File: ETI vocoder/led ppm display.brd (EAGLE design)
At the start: 49.2 x 51.4 mm, 29 parts, among them IC1 TL082P, IC2 LM3915N

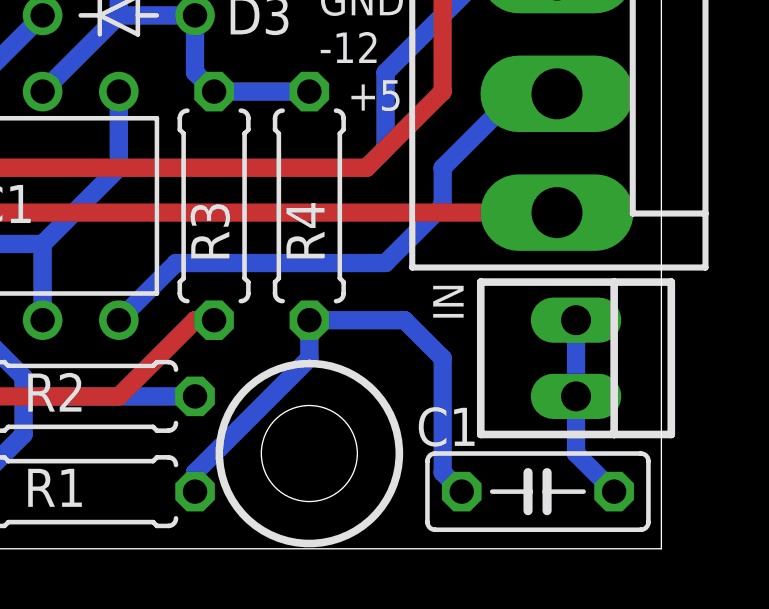
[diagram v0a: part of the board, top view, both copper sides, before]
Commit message: All ETI boards checked for caps and pots
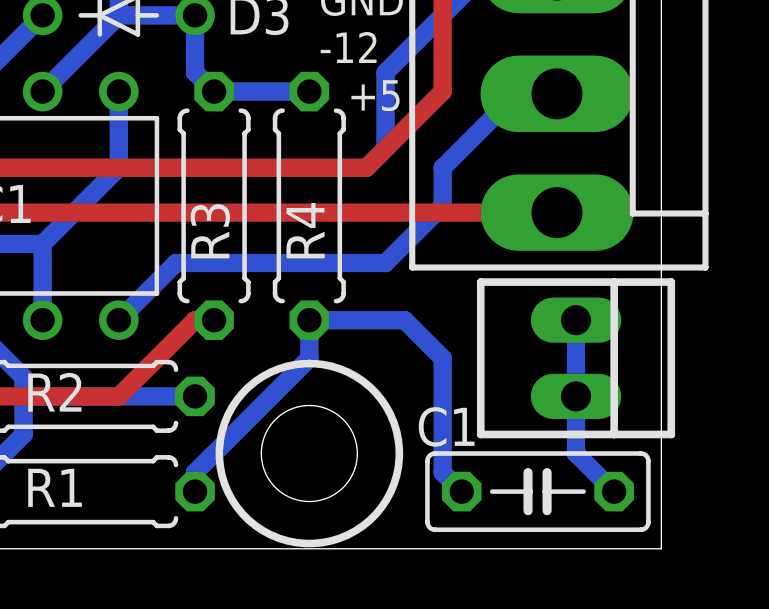
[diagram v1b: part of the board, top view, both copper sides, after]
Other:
- board text added: "+12V"
- board text added: "+5V"
- board text added: "-12V"
- board text added: "ETI Vocoder"
- board text added: "Input"
- board text added: "LED PPM v1.0"
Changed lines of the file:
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@@
 <?xml version="1.0" encoding="utf-8"?>
 <!DOCTYPE eagle SYSTEM "eagle.dtd">
-<eagle version="7.2.0">
+<eagle version="6.2">
 <drawing>
 <settings>
@@
 <setting verticaltext="up"/>
 </settings>
-<grid distance="0.0125" unitdist="inch" unit="mm" style="dots" multiple="1" display="yes" altdistance="0.025" altunitdist="inch" altunit="inch"/>
+<grid distance="0.0125" unitdist="inch" unit="inch" style="dots" multiple="1" display="yes" altdistance="0.025" altunitdist="inch" altunit="inch"/>
 <layers>
 <layer number="1" name="Top" color="4" fill="1" visible="yes" active="yes"/>
@@
 <text x="38.735" y="14.605" size="1.016" layer="21" font="vector">+5</text>
 <text x="10.16" y="25.0825" size="1.016" layer="21" font="vector">4V&amp;B</text>
+<text x="42.8625" y="22.5425" size="1.016" layer="26" font="vector" rot="MR0">+12V</text>
+<text x="42.8625" y="14.605" size="1.016" layer="26" font="vector" rot="MR0">-12V</text>
+<text x="42.8625" y="18.7325" size="1.016" layer="26" font="vector" rot="MR0">GND</text>
+<text x="42.8625" y="10.795" size="1.016" layer="26" font="vector" rot="MR0">+5V</text>
+<text x="44.1325" y="8.5725" size="1.016" layer="26" font="vector" rot="MR270">Input</text>
+<text x="11.7475" y="14.605" size="1.016" layer="26" font="vector" rot="MR90">ETI Vocoder</text>
+<text x="10.16" y="14.605" size="1.016" layer="26" font="vector" rot="MR90">LED PPM v1.0</text>
 </plain>
 <attributes>
@@
 </class>
 </classes>
-<designrules name="default">
+<designrules>
 <description language="de">&lt;b&gt;EAGLE Design Rules&lt;/b&gt;
 &lt;p&gt;
@@
 <pass name="Default">
 <param name="RoutingGrid" value="50mil"/>
-<param name="AutoGrid" value="1"/>
-<param name="Efforts" value="0"/>
-<param name="TopRouterVariant" value="1"/>
 <param name="tpViaShape" value="round"/>
-<param name="PrefDir.1" value="a"/>
+<param name="PrefDir.1" value="|"/>
 <param name="PrefDir.2" value="0"/>
 <param name="PrefDir.3" value="0"/>
@@
 <param name="PrefDir.14" value="0"/>
 <param name="PrefDir.15" value="0"/>
-<param name="PrefDir.16" value="a"/>
+<param name="PrefDir.16" value="-"/>
 <param name="cfVia" value="8"/>
 <param name="cfNonPref" value="5"/>
@@
 <attribute name="MF" value="MOLEX" x="46.355" y="6.35" size="1.778" layer="27" rot="R270" display="off"/>
 <attribute name="OC_FARNELL" value="1462926" x="46.355" y="6.35" size="1.778" layer="27" rot="R270" display="off"/>
-<attribute name="NAME" x="41.5925" y="8.89" size="1.016" layer="25" ratio="10" rot="R270"/>
 <attribute name="VALUE" x="41.275" y="8.89" size="1.016" layer="27" ratio="10" rot="R270"/>
 </element>

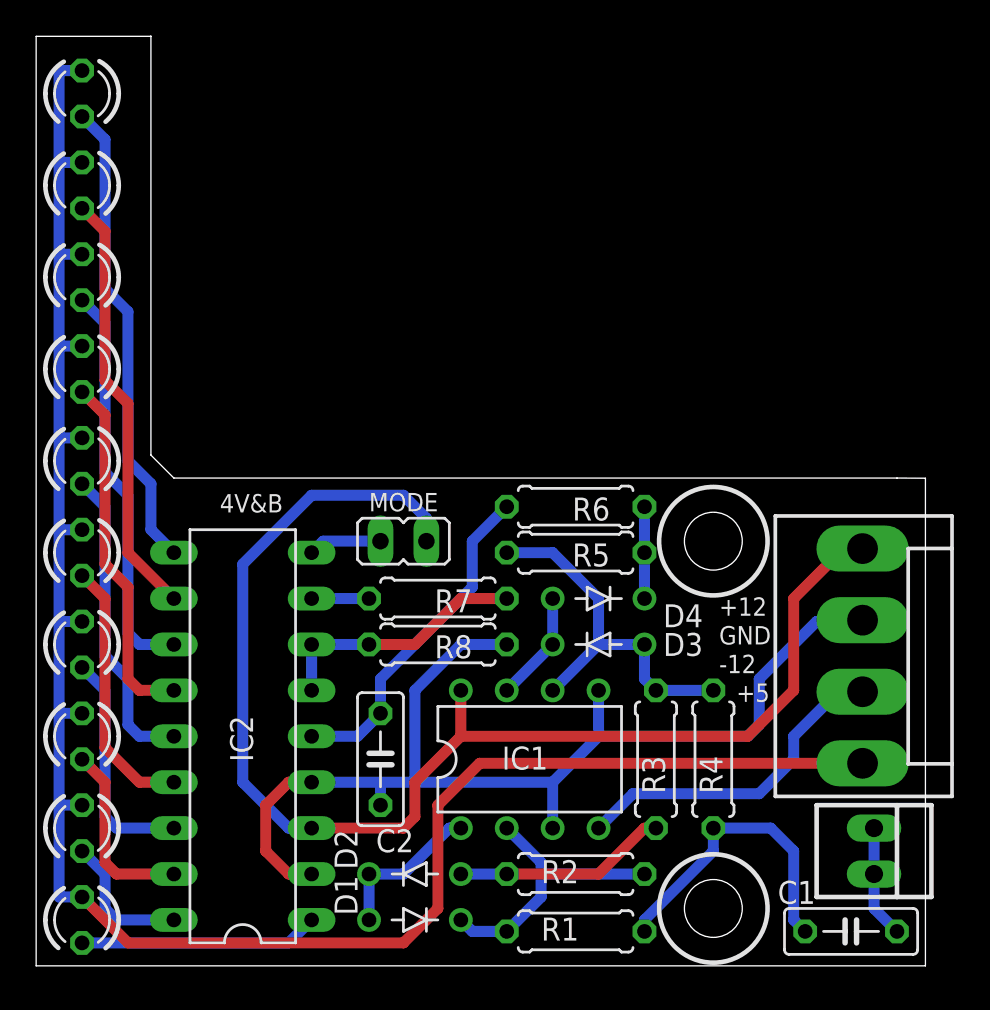
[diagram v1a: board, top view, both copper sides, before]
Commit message: Finished first of two halves of the universal voice board
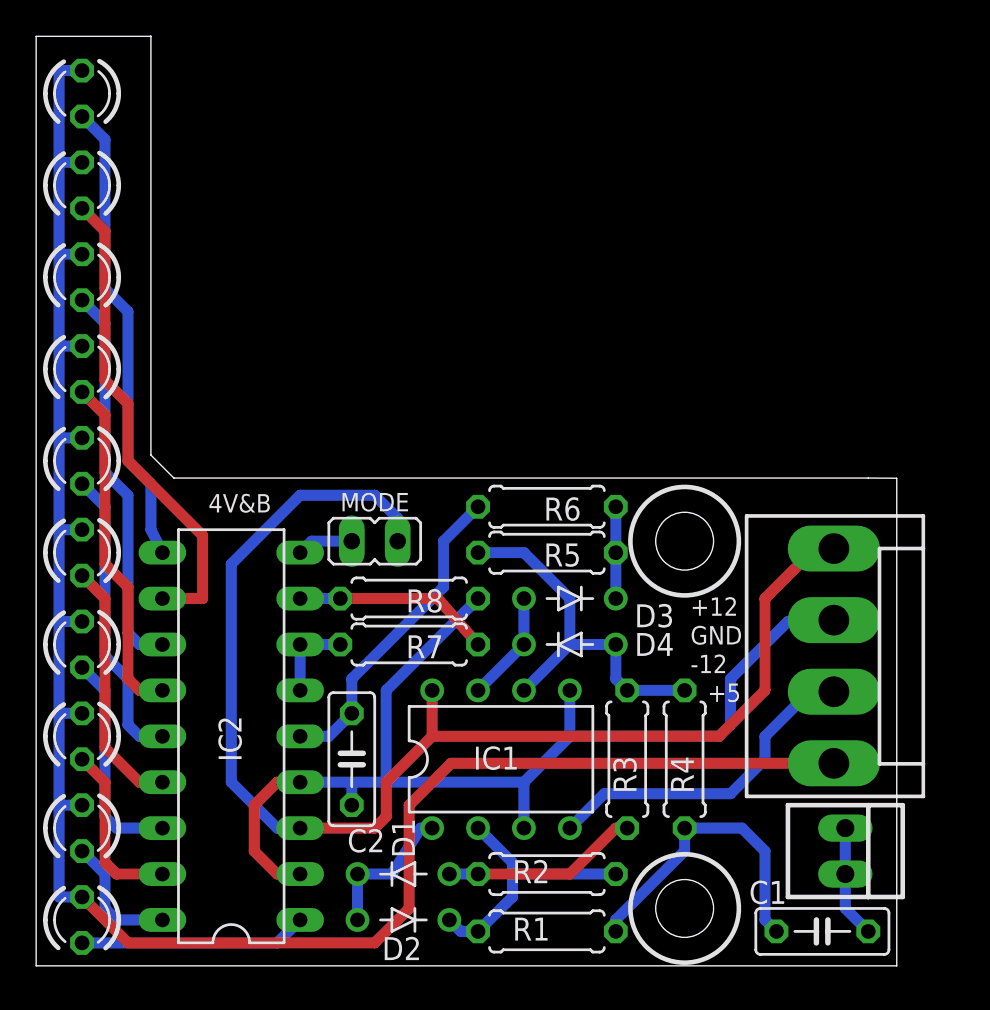
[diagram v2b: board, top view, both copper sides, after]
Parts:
- moved R7 3.00 mm to (20.6, 17.8)
- moved R8 3.00 mm to (20.6, 20.3)
- moved D3 3.00 mm to (29.5, 20.3), turned to 180 degrees
- moved D4 3.00 mm to (29.5, 17.8), turned to 0 degrees
- moved D1 2.62 mm to (20.3, 5.08), turned to 0 degrees
- moved D2 2.62 mm to (20.3, 2.54), turned to 180 degrees
- moved R4 1.59 mm to (35.9, 11.4)
- moved C2 1.59 mm to (17.5, 11.4)
- moved C1 1.59 mm to (43.5, 1.91)
- moved IC1 1.59 mm to (25.7, 11.4)
- moved IN 1.59 mm to (44.8, 6.35)
- moved MODE 1.59 mm to (18.7, 23.5)
- moved POWER 1.59 mm to (44.1, 17.1)
- moved R1 1.59 mm to (28.3, 1.91)
- moved R2 1.59 mm to (28.3, 5.08)
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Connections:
- removed net N$10: IC2.8, R7.2
- new net N$21: IC2.8, R7.1, R8.2
- net N$1: now also D1.A; no longer D2.A
- net N$2: now also D2.C; no longer D1.C
- net N$3: now also D1.C, D2.A; no longer D1.A, D2.C
- net N$4: now also D4.A; no longer D3.A
- net N$5: now also D3.C; no longer D4.C
- net N$7: now also D3.A, D4.C; no longer D3.C, D4.A
- net N$9: now also R7.2; no longer R7.1, R8.2
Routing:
- net N$21: track 0.00 -> 11.0 mm
- net N$9: track 14.4 -> 4.76 mm
- net N$10: track 3.17 -> 0.00 mm
- net N$19: track 23.7 -> 26.6 mm
- net +12V: track 74.0 -> 72.1 mm
- net +5V: track 110.1 -> 108.5 mm
- net MODE: track 4.07 -> 3.12 mm
- net N$8: track 18.7 -> 17.7 mm
- net N$2: track 15.8 -> 14.9 mm
- net N$1: track 11.8 -> 10.9 mm
- net N$18: track 22.3 -> 21.6 mm
- net N$17: track 19.7 -> 19.1 mm
- net N$16: track 17.2 -> 16.6 mm
- net N$15: track 14.7 -> 14.0 mm
- net N$14: track 12.9 -> 12.2 mm
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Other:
- board size 49.2 x 51.4 mm -> 47.6 x 51.4 mm
